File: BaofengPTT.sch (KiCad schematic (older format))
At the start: 8 parts, among them CON1 SJ1-3523N, CON2 SJ1-3523N, CON3 SJ1-3523N, CON4 SJ1-3523N, Q1 BSS138

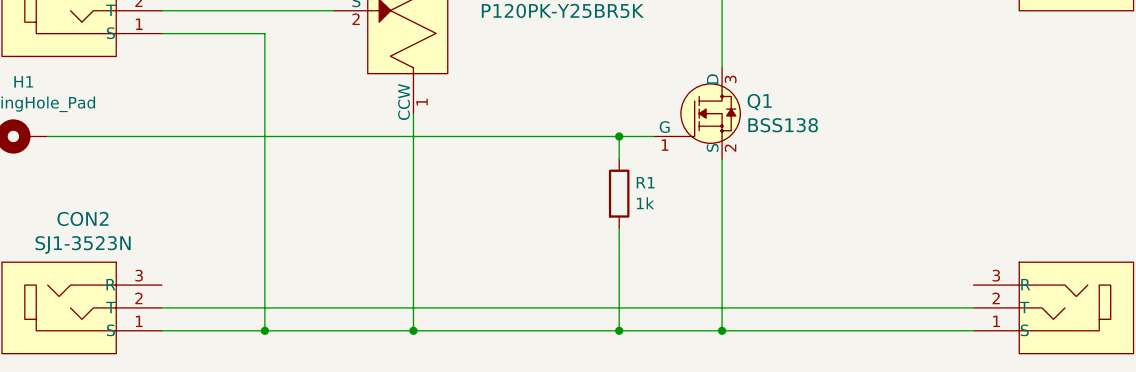
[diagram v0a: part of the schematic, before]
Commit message: added dc block capacitor
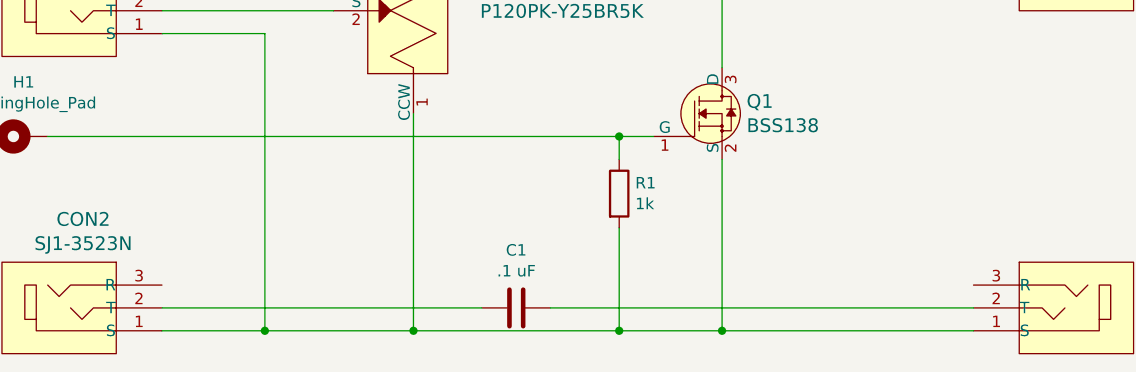
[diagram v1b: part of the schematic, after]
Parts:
- added C1: .1 uF, Capacitor_THT:C_Axial_L5.1mm_D3.1mm_P7.50mm_Horizontal, symbol Device:C
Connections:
- net at CON4.2 (T): now also C1.1; no longer CON2.2 (T)
- new net: C1.2, CON2.2 (T)
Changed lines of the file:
@@
 EESchema Schematic File Version 4
+LIBS:BaofengPTT-cache
 EELAYER 26 0
 EELAYER END
@@
 	4250 4250 4900 4250
 Wire Wire Line
-	7350 4150 3800 4150
-Wire Wire Line
 	3800 4250 4250 4250
 Connection ~ 4250 4250
@@
 	5800 3400 3300 3400
 Connection ~ 5800 3400
+$Comp
+L Device:C C1
+U 1 1 5F2CD361
+P 5350 4150
+F 0 "C1" V 5098 4150 50  0000 C CNN
+F 1 ".1 uF" V 5189 4150 50  0000 C CNN
+F 2 "Capacitor_THT:C_Axial_L5.1mm_D3.1mm_P7.50mm_Horizontal" H 5388 4000 50  0001 C CNN
+F 3 "~" H 5350 4150 50  0001 C CNN
+	1    5350 4150
+	0    1    1    0
+$EndComp
+Wire Wire Line
+	7350 4150 5500 4150
+Wire Wire Line
+	5200 4150 3800 4150
 $EndSCHEMATC

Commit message: added resitor to lower input level to sound card, placed top side coppor pour
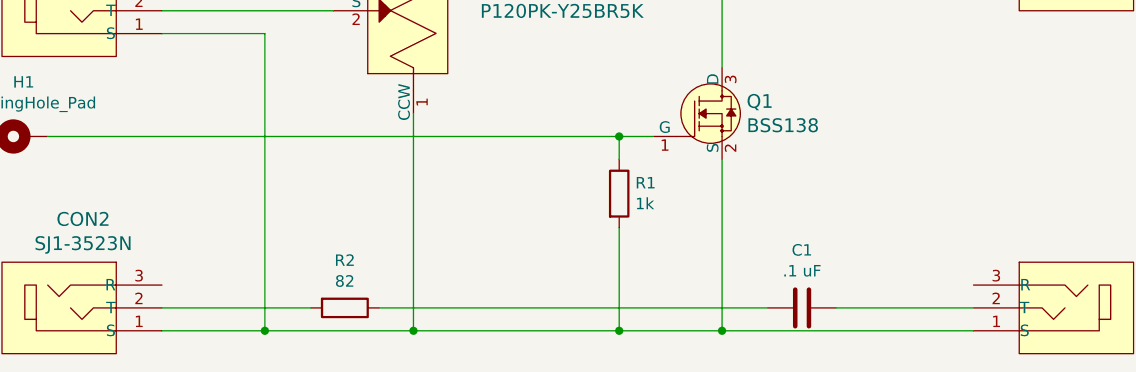
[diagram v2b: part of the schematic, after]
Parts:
- added R2: 82, Resistor_THT:R_Axial_DIN0207_L6.3mm_D2.5mm_P7.62mm_Horizontal, symbol Device:R
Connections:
- net at CON2.2 (T): now also R2.2; no longer C1.2
- new net: C1.2, R2.1
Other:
- moved on the sheet: C1
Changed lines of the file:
@@
 L Device:C C1
 U 1 1 5F2CD361
-P 5350 4150
-F 0 "C1" V 5098 4150 50  0000 C CNN
-F 1 ".1 uF" V 5189 4150 50  0000 C CNN
-F 2 "Capacitor_THT:C_Axial_L5.1mm_D3.1mm_P7.50mm_Horizontal" H 5388 4000 50  0001 C CNN
-F 3 "~" H 5350 4150 50  0001 C CNN
-	1    5350 4150
+P 6600 4150
+F 0 "C1" V 6348 4150 50  0000 C CNN
+F 1 ".1 uF" V 6439 4150 50  0000 C CNN
+F 2 "Capacitor_THT:C_Axial_L5.1mm_D3.1mm_P7.50mm_Horizontal" H 6638 4000 50  0001 C CNN
+F 3 "~" H 6600 4150 50  0001 C CNN
+	1    6600 4150
 	0    1    1    0
 $EndComp
 Wire Wire Line
-	7350 4150 5500 4150
+	7350 4150 6750 4150
+$Comp
+L Device:R R2
+U 1 1 5F2DFA80
+P 4600 4150
+F 0 "R2" V 4393 4150 50  0000 C CNN
+F 1 "82" V 4484 4150 50  0000 C CNN
+F 2 "Resistor_THT:R_Axial_DIN0207_L6.3mm_D2.5mm_P7.62mm_Horizontal" V 4530 4150 50  0001 C CNN
+F 3 "~" H 4600 4150 50  0001 C CNN
+	1    4600 4150
+	0    1    1    0
+$EndComp
 Wire Wire Line
-	5200 4150 3800 4150
+	3800 4150 4450 4150
+Wire Wire Line
+	4750 4150 6450 4150
 $EndSCHEMATC

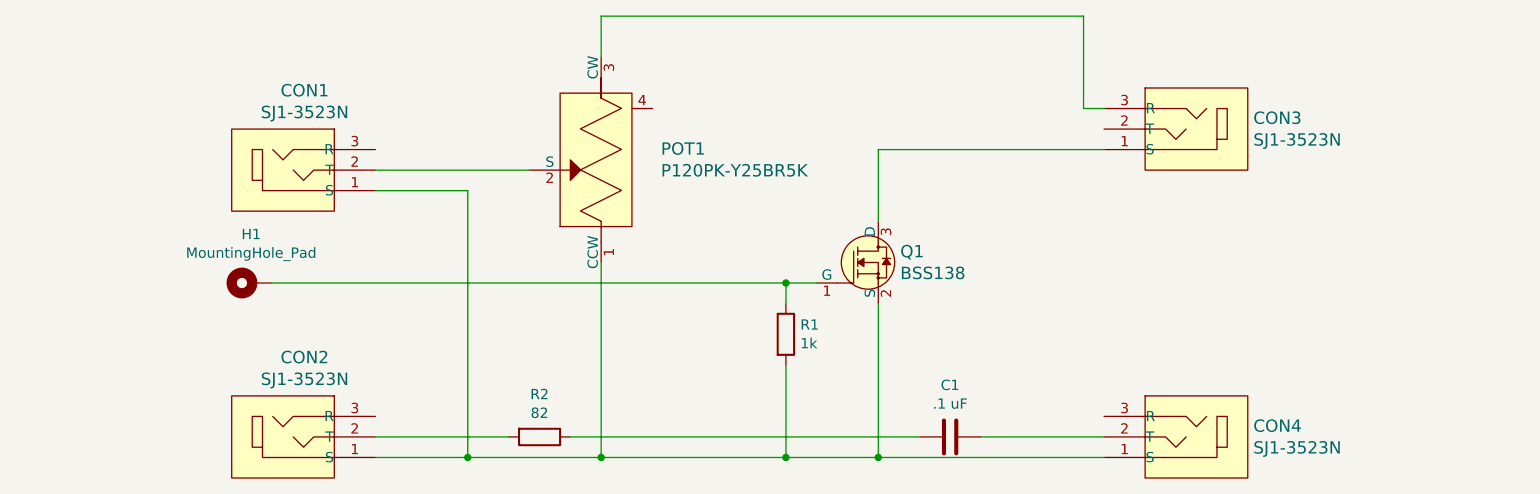
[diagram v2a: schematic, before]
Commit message: added notes to schematic
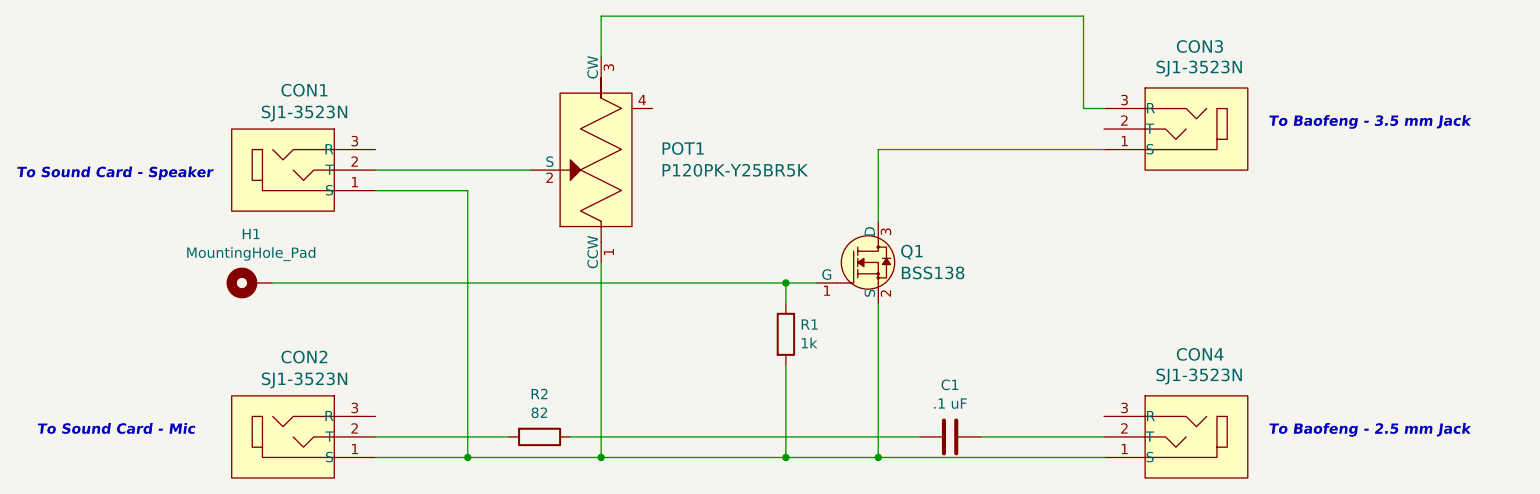
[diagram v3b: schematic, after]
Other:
- note added: "To Baofeng - 2.5 mm Jack"
- note added: "To Baofeng - 3.5 mm Jack"
- note added: "To Sound Card - Mic"
- note added: "To Sound Card - Speaker"
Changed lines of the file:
@@
 U 1 1 5F28CB86
 P 7750 2650
-F 0 "CON3" H 7423 2703 60  0000 R CNN
-F 1 "SJ1-3523N" H 7423 2597 60  0000 R CNN
+F 0 "CON3" H 7800 3050 60  0000 R CNN
+F 1 "SJ1-3523N" H 7900 2950 60  0000 R CNN
 F 2 "digikey-footprints:Headphone_Jack_3.5mm_SJ1-3523N" H 7950 2850 60  0001 L CNN
 F 3 "https://www.cui.com/product/resource/digikeypdf/sj1-352xn_series.pdf" H 7950 2950 60  0001 L CNN
@@
 U 1 1 5F28CCA2
 P 7750 4150
-F 0 "CON4" H 7423 4203 60  0000 R CNN
-F 1 "SJ1-3523N" H 7423 4097 60  0000 R CNN
+F 0 "CON4" H 7800 4550 60  0000 R CNN
+F 1 "SJ1-3523N" H 7900 4450 60  0000 R CNN
 F 2 "digikey-footprints:Headphone_Jack_3.5mm_SJ1-3523N" H 7950 4350 60  0001 L CNN
 F 3 "https://www.cui.com/product/resource/digikeypdf/sj1-352xn_series.pdf" H 7950 4450 60  0001 L CNN
@@
 Wire Wire Line
 	4750 4150 6450 4150
+Text Notes 2050 2900 0    50   Italic 10
+To Sound Card - Speaker
+Text Notes 2150 4150 0    50   Italic 10
+To Sound Card - Mic
+Text Notes 8150 2650 0    50   Italic 10
+To Baofeng - 3.5 mm Jack
+Text Notes 8150 4150 0    50   Italic 10
+To Baofeng - 2.5 mm Jack
 $EndSCHEMATC
